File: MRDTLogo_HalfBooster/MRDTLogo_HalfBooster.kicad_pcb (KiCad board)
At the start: 2 copper layers, 61 x 99.8 mm, 6 parts, among them U1 TM4C129E_Launchpad

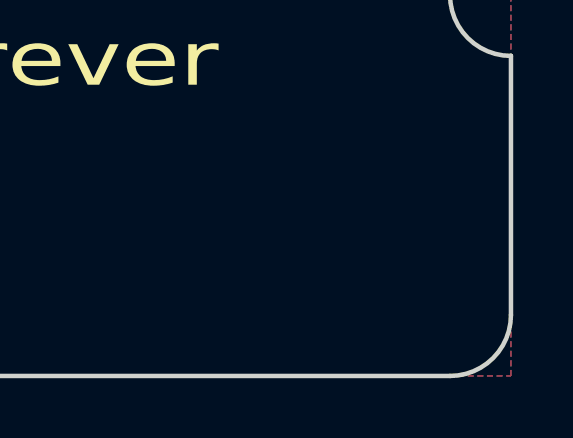
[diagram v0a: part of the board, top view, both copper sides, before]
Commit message: fixed soldermask
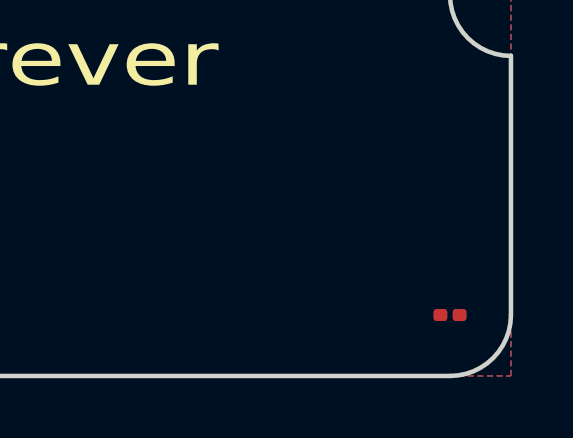
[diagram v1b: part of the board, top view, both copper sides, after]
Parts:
- added REF**: R_0201_0603Metric, Resistor_SMD:R_0201_0603Metric, F.Cu at (178.3, 114.8)
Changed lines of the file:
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@@
-(kicad_pcb (version 20171130) (host pcbnew "(5.0.0)")
+(kicad_pcb (version 20171130) (host pcbnew "(5.0.2)-1")
   (general
     (thickness 1.6)
@@
     (tracks 1)
     (zones 0)
-    (modules 6)
+    (modules 7)
     (nets 40)
   )
@@
     (pad_drill 0.762)
     (pad_to_mask_clearance 0.2)
+    (solder_mask_min_width 0.25)
     (aux_axis_origin 0 0)
     (visible_elements 7FFFFFFF)
@@
       (outputformat 1)
       (mirror false)
-      (drillshape 1)
+      (drillshape 0)
       (scaleselection 1)
-      (outputdirectory ""))
+      (outputdirectory "Gerbs/"))
   )
   (net 0 "")
@@
       (xy 7.622799 -13.72785) (xy 7.673011 -13.7691) (xy 7.759835 -13.820612) (xy 7.790976 -13.820251)) (layer F.SilkS) (width 0.01))
   )
+  (module Resistor_SMD:R_0201_0603Metric (layer F.Cu)
+    (at 178.308 114.808)
+    (descr "Resistor SMD 0201 (0603 Metric), square (rectangular) end terminal, IPC_7351 nominal, (Body size source: https://www.vishay.com/docs/20052/crcw0201e3.pdf), generated with kicad-footprint-generator")
+    (tags resistor)
+    (attr smd)
+    (fp_text reference REF** (at 0 -1.05) (layer F.SilkS) hide
+      (effects (font (size 1 1) (thickness 0.15)))
+    )
+    (fp_text value R_0201_0603Metric (at 0 1.05) (layer F.Fab)
+      (effects (font (size 1 1) (thickness 0.15)))
+    )
+    (fp_text user %R (at 0 -0.68) (layer F.Fab)
+      (effects (font (size 0.25 0.25) (thickness 0.04)))
+    )
+    (fp_line (start 0.7 0.35) (end -0.7 0.35) (layer F.CrtYd) (width 0.05))
+    (fp_line (start 0.7 -0.35) (end 0.7 0.35) (layer F.CrtYd) (width 0.05))
+    (fp_line (start -0.7 -0.35) (end 0.7 -0.35) (layer F.CrtYd) (width 0.05))
+    (fp_line (start -0.7 0.35) (end -0.7 -0.35) (layer F.CrtYd) (width 0.05))
+    (fp_line (start 0.3 0.15) (end -0.3 0.15) (layer F.Fab) (width 0.1))
+    (fp_line (start 0.3 -0.15) (end 0.3 0.15) (layer F.Fab) (width 0.1))
+    (fp_line (start -0.3 -0.15) (end 0.3 -0.15) (layer F.Fab) (width 0.1))
+    (fp_line (start -0.3 0.15) (end -0.3 -0.15) (layer F.Fab) (width 0.1))
+    (pad 2 smd roundrect (at 0.32 0) (size 0.46 0.4) (layers F.Cu F.Mask) (roundrect_rratio 0.25))
+    (pad 1 smd roundrect (at -0.32 0) (size 0.46 0.4) (layers F.Cu F.Mask) (roundrect_rratio 0.25))
+    (pad "" smd roundrect (at 0.345 0) (size 0.318 0.36) (layers F.Paste) (roundrect_rratio 0.25))
+    (pad "" smd roundrect (at -0.345 0) (size 0.318 0.36) (layers F.Paste) (roundrect_rratio 0.25))
+    (model ${KISYS3DMOD}/Resistor_SMD.3dshapes/R_0201_0603Metric.wrl
+      (at (xyz 0 0 0))
+      (scale (xyz 1 1 1))
+      (rotate (xyz 0 0 0))
+    )
+  )
   (gr_text "Today. Tomorrow. Forever" (at 149.733 106.299) (layer F.SilkS)
